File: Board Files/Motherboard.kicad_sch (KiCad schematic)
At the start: 77 parts, among them P1 72-Pin Connector, P2 PowerSw, P3 ResetSw, P4 Controller_Port, P6 RF-Mod, Q1 2SA937, Q2 2SC2021, T1 08RB01, U1 6116 (WRAM), U2 74HC373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

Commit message: added start of usb C power supply
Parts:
- removed P6: RF-Mod, Toploader:RF-MOD, symbol Motherboard:RF-Mod
- added C39: 1uF, symbol Device:C_Polarized_Small
- added J1: USB_C_Receptacle_PowerOnly_6P, symbol Connector:USB_C_Receptacle_PowerOnly_6P
- added R11, R12: 5.1K, symbol Device:R
- added U10: IP2721, Package_SO:TSSOP-16_4.4x5mm_P0.65mm, symbol Interface_USB:IP2721
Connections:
- net GND: now also C39.2, J1.A12 (GND), J1.B12 (GND), J1.S1 (SHIELD), R11.2, R12.2, U10.11 (SEL), U10.5 (GND)
- new net: C39.1, J1.A9 (VBUS), J1.B9 (VBUS), U10.2 (VIN)
- new net: J1.A5 (CC1), R12.1, U10.13 (CC1)
- new net: J1.B5 (CC2), R11.1, U10.12 (CC2)
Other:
- note removed: "RF MODULATOR"

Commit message: Power supply complete?
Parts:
- removed ACPLUG1: (no value), Toploader:AC-JACK, symbol Connector:Jack-DC
- removed C12: 10nF, Capacitor_THT:C_Disc_D3.0mm_W1.6mm_P2.50mm, symbol Device:C
- removed C13: 1500uF, Capacitor_THT:CP_Radial_D12.5mm_P5.00mm, symbol Device:C_Polarized
- removed C14: 1uF, Capacitor_THT:CP_Radial_D5.0mm_P2.50mm, symbol Device:C_Polarized
- removed DB1: RC203, Toploader:Rectifier, symbol Device:D_Bridge_+-AA
- removed T1: 08RB01, Toploader:Inductor, symbol Device:L_Coupled
- removed U9: L7805, Connector_PinHeader_2.54mm:PinHeader_1x03_P2.54mm_Vertical, symbol Regulator_Linear:L7805
- added C12: 10uF, symbol Device:C_Polarized_Small
- added Q3: AO3400A, Package_TO_SOT_SMD:SOT-23, symbol Transistor_FET:AO3400A
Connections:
- net GND: now also C12.2
- net VCC: now also P2.2
- net at P2.1: now also U10.16 (VBUS), C12.1, Q3.2 (S)
- net at C39.1, J1.A9 (VBUS), J1.B9 (VBUS)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: now also Q3.3 (D)
- net at U10.1 (VBUSG): now also Q3.1 (G)
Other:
- note added: "USB-C Power"
- note removed: "RECTIFIER CIRCUIT"
- moved on the sheet: C10, C11, C2, C3, C39, C4, C5, C7, C8, C9, FC1, FC2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

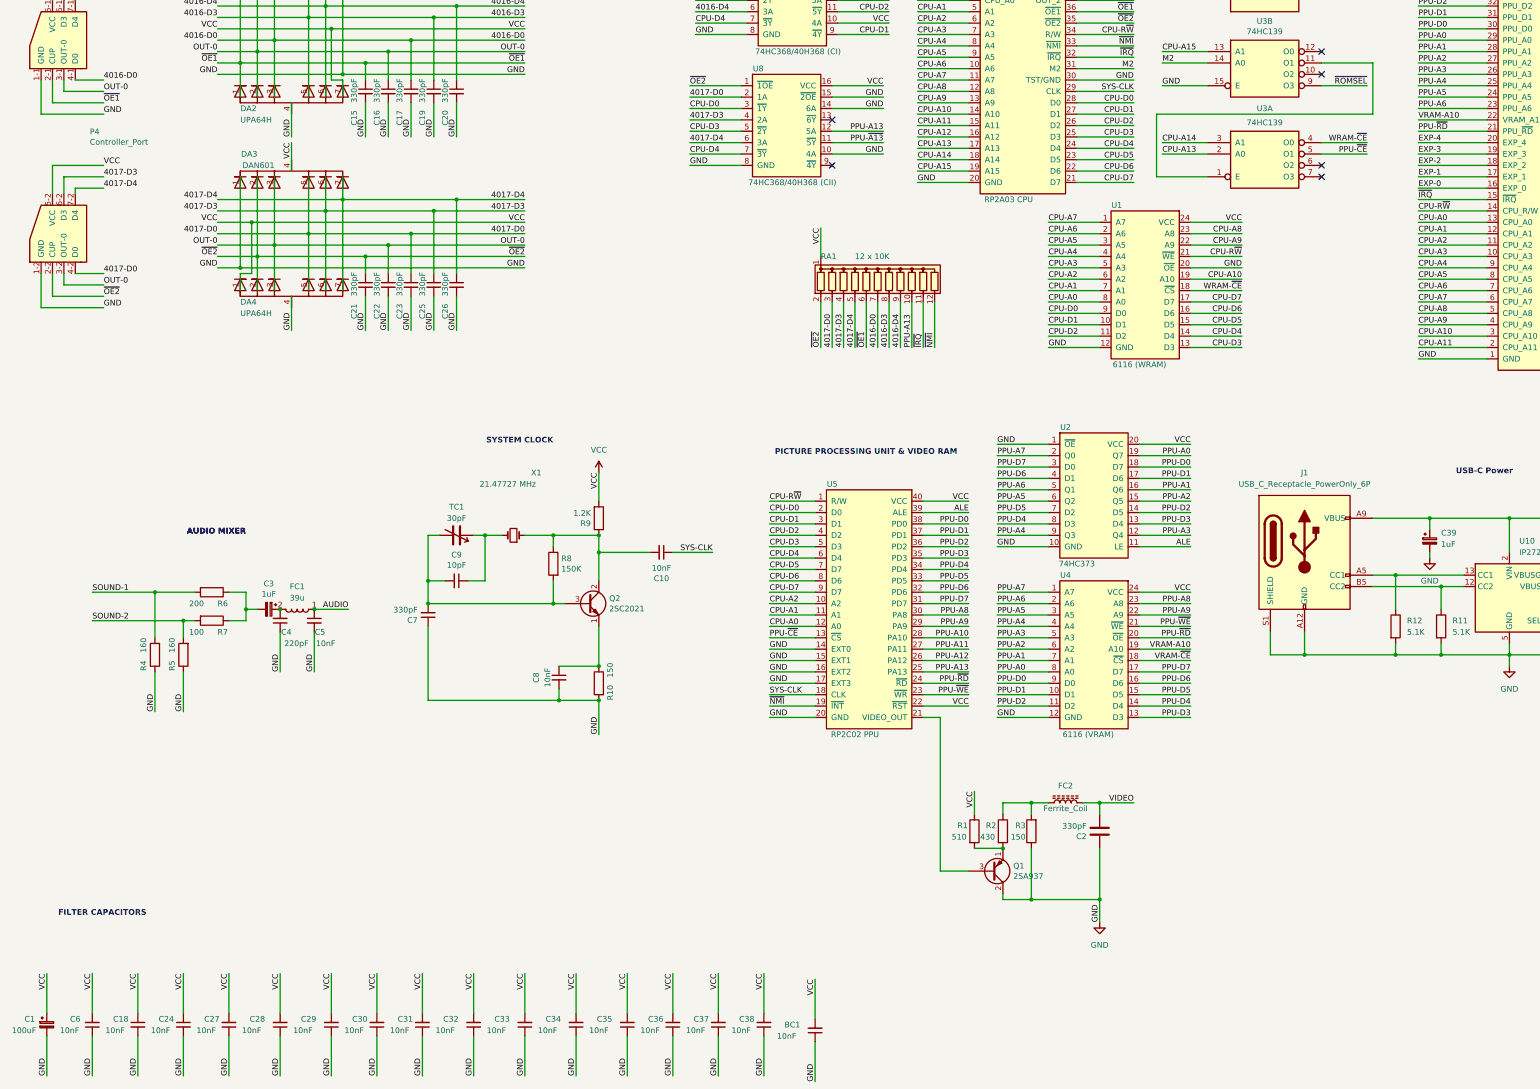
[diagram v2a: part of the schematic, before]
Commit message: added video and audio
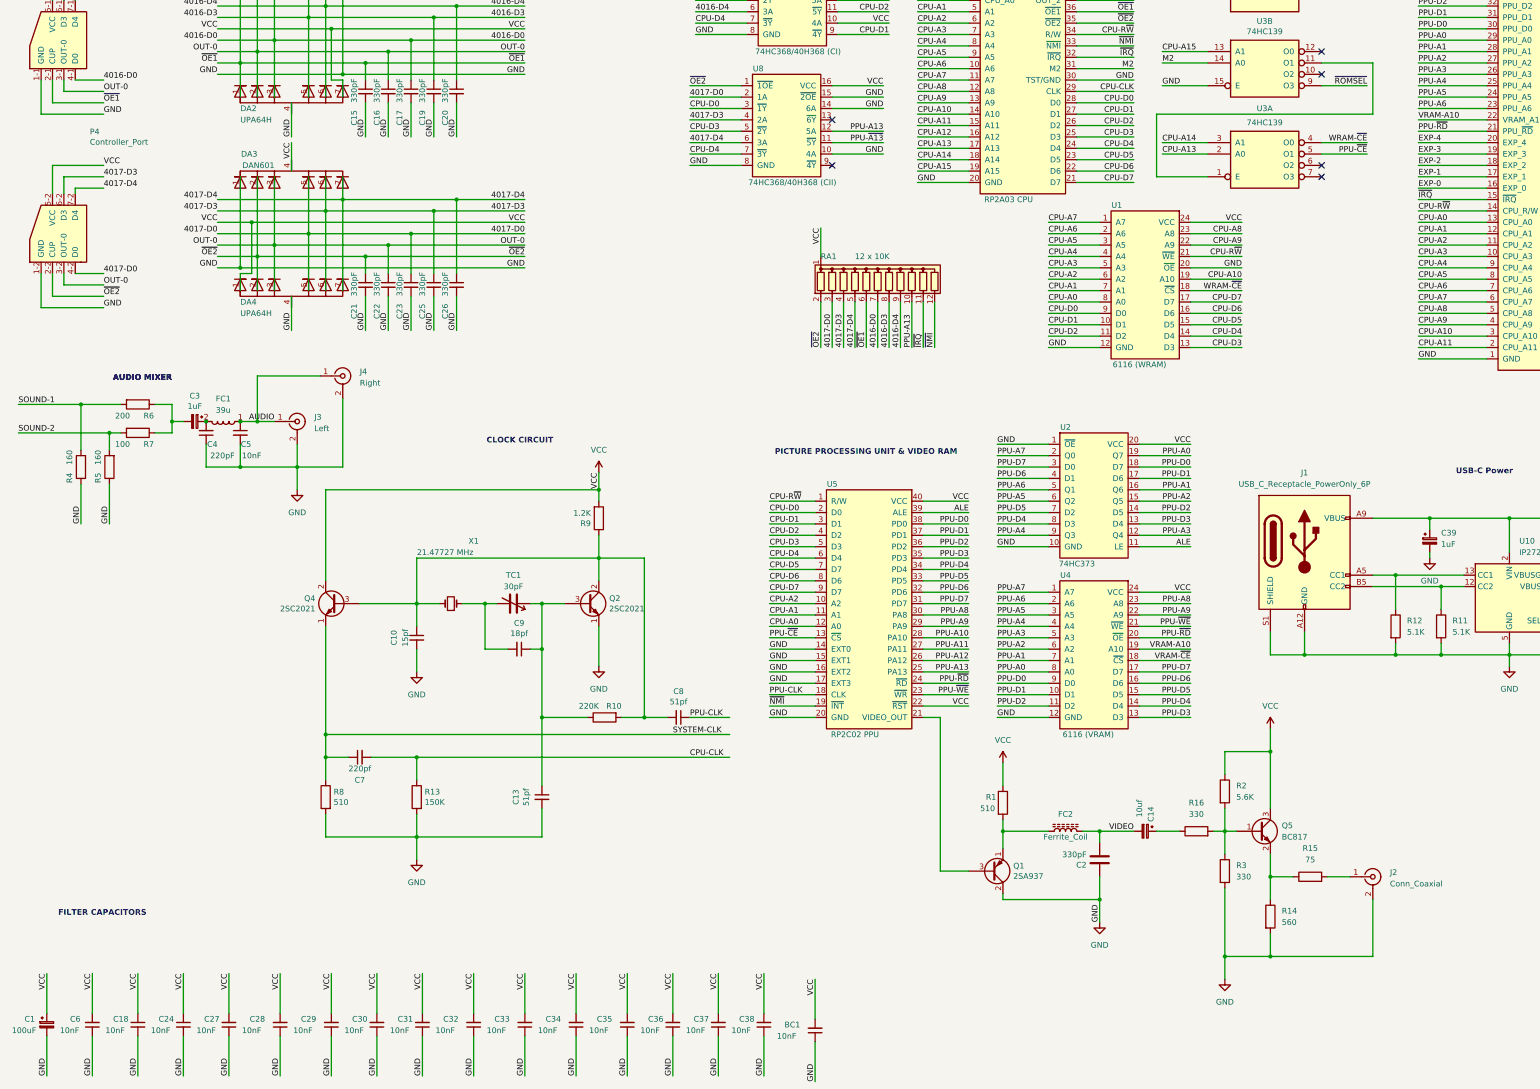
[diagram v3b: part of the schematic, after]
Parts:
- removed C10: 10nF, Capacitor_THT:C_Disc_D3.0mm_W1.6mm_P2.50mm, symbol Device:C_Small
- added C13, C8: 51pf, Capacitor_THT:C_Disc_D3.0mm_W2.0mm_P2.50mm, symbol Device:C_Small
- added C14: 10uf, Capacitor_THT:CP_Radial_D5.0mm_P2.50mm, symbol Device:C_Polarized_Small
- added J2: Conn_Coaxial, Connector_Coaxial:BNC_Win_364A2x95_Horizontal, symbol Connector:Conn_Coaxial
- added J3: Left, Connector_Coaxial:BNC_Win_364A2x95_Horizontal, symbol Connector:Conn_Coaxial
- added J4: Right, Connector_Coaxial:BNC_Win_364A2x95_Horizontal, symbol Connector:Conn_Coaxial
- added Q4: 2SC2021, Package_TO_SOT_THT:TO-126-3_Vertical, symbol Device:Q_NPN_ECB
- added Q5: BC817, Package_TO_SOT_SMD:SOT-23, symbol Transistor_BJT:BC817
- added R13: 150K, Resistor_THT:R_Axial_DIN0207_L6.3mm_D2.5mm_P10.16mm_Horizontal, symbol Device:R
- added R14: 560, symbol Device:R
- added R15: 75, symbol Device:R
- added R16: 330, symbol Device:R
- C10: renamed from C8; value 10nF -> 15pf
- C7: value 330pF -> 220pf; footprint Capacitor_THT:C_Disc_D3.0mm_W1.6mm_P2.50mm -> Capacitor_THT:C_Disc_D3.0mm_W2.0mm_P2.50mm
- C9: value 10pF -> 18pf
- R10: value 150 -> 220K
- R2: value 430 -> 5.6K; footprint Resistor_THT:R_Axial_DIN0207_L6.3mm_D2.5mm_P10.16mm_Horizontal -> (none)
- R3: value 150 -> 330; footprint Resistor_THT:R_Axial_DIN0207_L6.3mm_D2.5mm_P10.16mm_Horizontal -> (none)
- R8: value 150K -> 510
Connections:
- net AUDIO: now also J3.1 (In), J4.1 (In)
- net GND: now also Q2.1 (E), R3.2, R8.2, C13.2, J2.2 (Ext), J3.2 (Ext), J4.2 (Ext), R13.2, R14.2; no longer C7.1, R10.2, R3.1
- net SYSTEM-CLK: now also C7.1, R8.1, Q4.1 (E)
- net VCC: now also R2.1, Q4.2 (C), Q5.3 (C)
- net VIDEO: now also C14.2
- net at Q1.1 (E), R1.2: now also FC2.1; no longer R2.2
- net at C9.1, TC1.1: now also Q2.3 (B), R10.1, C13.1; no longer X1.2
- net at Q2.2 (C), R9.1: now also C10.1, R10.2, X1.2, C8.2, Q4.3 (B); no longer R8.1, X1.1
- net SYS-CLK renamed CPU-CLK
- net CPU-CLK: now also C7.2, R13.1; no longer U5.18 (CLK)
- new net: C9.2, TC1.2, X1.1
- new net: Q5.1 (B), R16.2, R2.2, R3.1
- new net: C14.1, R16.1
- new net: Q5.2 (E), R14.1, R15.1
- new net: J2.1 (In), R15.2
- new net PPU-CLK: C8.1, U5.18 (CLK)
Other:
- note added: "CLOCK CIRCUIT"
- note removed: "SYSTEM CLOCK"
- moved on the sheet: C10, C2, C3, C4, C5, C9, FC1, FC2, R1, R10, R4, R5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

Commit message: little bit of routing
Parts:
- C12, C39: footprint (none) -> Capacitor_THT:CP_Radial_D5.0mm_P2.50mm
- J1: footprint (none) -> Connector_USB:USB_C_Receptacle_GCT_USB4125-xx-x-0190_6P_TopMnt_Horizontal
- R11, R12, R14, R15, R16, R2, R3: footprint (none) -> Resistor_THT:R_Axial_DIN0207_L6.3mm_D2.5mm_P10.16mm_Horizontal
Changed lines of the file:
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@@
 			)
 		)
-		(property "Footprint" ""
+		(property "Footprint" "Resistor_THT:R_Axial_DIN0207_L6.3mm_D2.5mm_P10.16mm_Horizontal"
 			(at 283.972 214.63 90)
 			(effects
@@
 			)
 		)
-		(property "Footprint" ""
+		(property "Footprint" "Capacitor_THT:CP_Radial_D5.0mm_P2.50mm"
 			(at 374.65 176.53 0)
 			(effects
@@
 			)
 		)
-		(property "Footprint" ""
+		(property "Footprint" "Resistor_THT:R_Axial_DIN0207_L6.3mm_D2.5mm_P10.16mm_Horizontal"
 			(at 279.4 225.298 90)
 			(effects
@@
 			)
 		)
-		(property "Footprint" ""
+		(property "Footprint" "Resistor_THT:R_Axial_DIN0207_L6.3mm_D2.5mm_P10.16mm_Horizontal"
 			(at 294.132 242.57 90)
 			(effects
@@
 			)
 		)
-		(property "Footprint" ""
+		(property "Footprint" "Capacitor_THT:CP_Radial_D5.0mm_P2.50mm"
 			(at 331.47 158.75 0)
 			(effects
@@
 			)
 		)
-		(property "Footprint" ""
+		(property "Footprint" "Resistor_THT:R_Axial_DIN0207_L6.3mm_D2.5mm_P10.16mm_Horizontal"
 			(at 322.072 177.8 90)
 			(effects
@@
 			)
 		)
-		(property "Footprint" ""
+		(property "Footprint" "Resistor_THT:R_Axial_DIN0207_L6.3mm_D2.5mm_P10.16mm_Horizontal"
 			(at 304.8 235.458 90)
 			(effects
@@
 			)
 		)
-		(property "Footprint" ""
+		(property "Footprint" "Connector_USB:USB_C_Receptacle_GCT_USB4125-xx-x-0190_6P_TopMnt_Horizontal"
 			(at 307.34 158.75 0)
 			(effects
@@
 			)
 		)
-		(property "Footprint" ""
+		(property "Footprint" "Resistor_THT:R_Axial_DIN0207_L6.3mm_D2.5mm_P10.16mm_Horizontal"
 			(at 283.972 232.41 90)
 			(effects
@@
 			)
 		)
-		(property "Footprint" ""
+		(property "Footprint" "Resistor_THT:R_Axial_DIN0207_L6.3mm_D2.5mm_P10.16mm_Horizontal"
 			(at 332.232 177.8 90)
 			(effects

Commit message: Progress
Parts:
- C27: footprint Capacitor_THT:C_Disc_D5.0mm_W2.5mm_P5.00mm -> Capacitor_THT:C_Disc_D3.0mm_W2.0mm_P2.50mm
- J2: value Conn_Coaxial -> Composite; footprint Connector_Coaxial:BNC_Win_364A2x95_Horizontal -> Samacsys:PJRAN1X1U03AUX
- J3, J4: footprint Connector_Coaxial:BNC_Win_364A2x95_Horizontal -> Samacsys:PJRAN1X1U03AUX
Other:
- moved on the sheet: C29
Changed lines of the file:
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@@
 	(wire
 		(pts
+			(xy 86.36 271.78) (xy 86.36 278.13)
+		)
+		(stroke
+			(width 0)
+			(type default)
+		)
+	)
+	(wire
+		(pts
 			(xy 246.38 87.63) (xy 257.81 87.63)
 		)
@@
 	(wire
 		(pts
+			(xy 86.36 262.89) (xy 86.36 255.27)
+		)
+		(stroke
+			(width 0)
+			(type default)
+		)
+	)
+	(wire
+		(pts
 			(xy 252.73 35.56) (xy 265.43 35.56)
 		)
@@
 	(wire
 		(pts
-			(xy 86.36 255.27) (xy 86.36 264.16)
+			(xy 81.28 262.89) (xy 86.36 262.89)
+		)
+		(stroke
+			(width 0)
+			(type default)
+		)
+	)
+	(wire
+		(pts
+			(xy 81.28 262.89) (xy 81.28 264.16)
 		)
 		(stroke
@@
 	(wire
 		(pts
-			(xy 86.36 269.24) (xy 86.36 278.13)
+			(xy 81.28 269.24) (xy 81.28 271.78)
 		)
 		(stroke
@@
 	(wire
 		(pts
+			(xy 81.28 271.78) (xy 86.36 271.78)
+		)
+		(stroke
+			(width 0)
+			(type default)
+		)
+	)
+	(wire
+		(pts
 			(xy 377.19 82.55) (xy 392.43 82.55)
 		)
@@
 			)
 		)
-		(property "Footprint" "Capacitor_THT:C_Disc_D5.0mm_W2.5mm_P5.00mm"
+		(property "Footprint" "Capacitor_THT:C_Disc_D3.0mm_W2.0mm_P2.50mm"
 			(at 63.5 266.7 0)
 			(effects
@@
 	(symbol
 		(lib_id "Device:C_Small")
-		(at 86.36 266.7 180)
+		(at 81.28 266.7 180)
 		(unit 1)
 		(exclude_from_sim no)
@@
 		(dnp no)
 		(property "Reference" "C29"
-			(at 81.28 265.43 0)
+			(at 76.2 265.43 0)
 			(effects
 				(font
@@
 		)
 		(property "Value" "10nF"
-			(at 80.01 267.97 0)
+			(at 74.93 267.97 0)
 			(effects
 				(font
@@
 		)
 		(property "Footprint" "Capacitor_THT:C_Disc_D3.0mm_W2.0mm_P2.50mm"
-			(at 86.36 266.7 0)
+			(at 81.28 266.7 0)
 			(effects
 				(font
@@
 		)
 		(property "Datasheet" "~"
-			(at 86.36 266.7 0)
+			(at 81.28 266.7 0)
 			(effects
 				(font
@@
 		)
 		(property "Description" ""
-			(at 86.36 266.7 0)
+			(at 81.28 266.7 0)
 			(effects
 				(font
@@
 			)
 		)
-		(property "Footprint" "Connector_Coaxial:BNC_Win_364A2x95_Horizontal"
+		(property "Footprint" "Samacsys:PJRAN1X1U03AUX"
 			(at 88.9 121.92 0)
 			(effects
@@
 			)
 		)
-		(property "Footprint" "Connector_Coaxial:BNC_Win_364A2x95_Horizontal"
+		(property "Footprint" "Samacsys:PJRAN1X1U03AUX"
 			(at 78.74 132.08 0)
 			(effects
@@
 			)
 		)
-		(property "Value" "Conn_Coaxial"
+		(property "Value" "Composite"
 			(at 322.58 235.2431 0)
 			(effects
@@
 			)
 		)
-		(property "Footprint" "Connector_Coaxial:BNC_Win_364A2x95_Horizontal"
+		(property "Footprint" "Samacsys:PJRAN1X1U03AUX"
 			(at 318.77 233.68 0)
 			(effects
